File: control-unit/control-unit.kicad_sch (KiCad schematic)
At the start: 23 parts

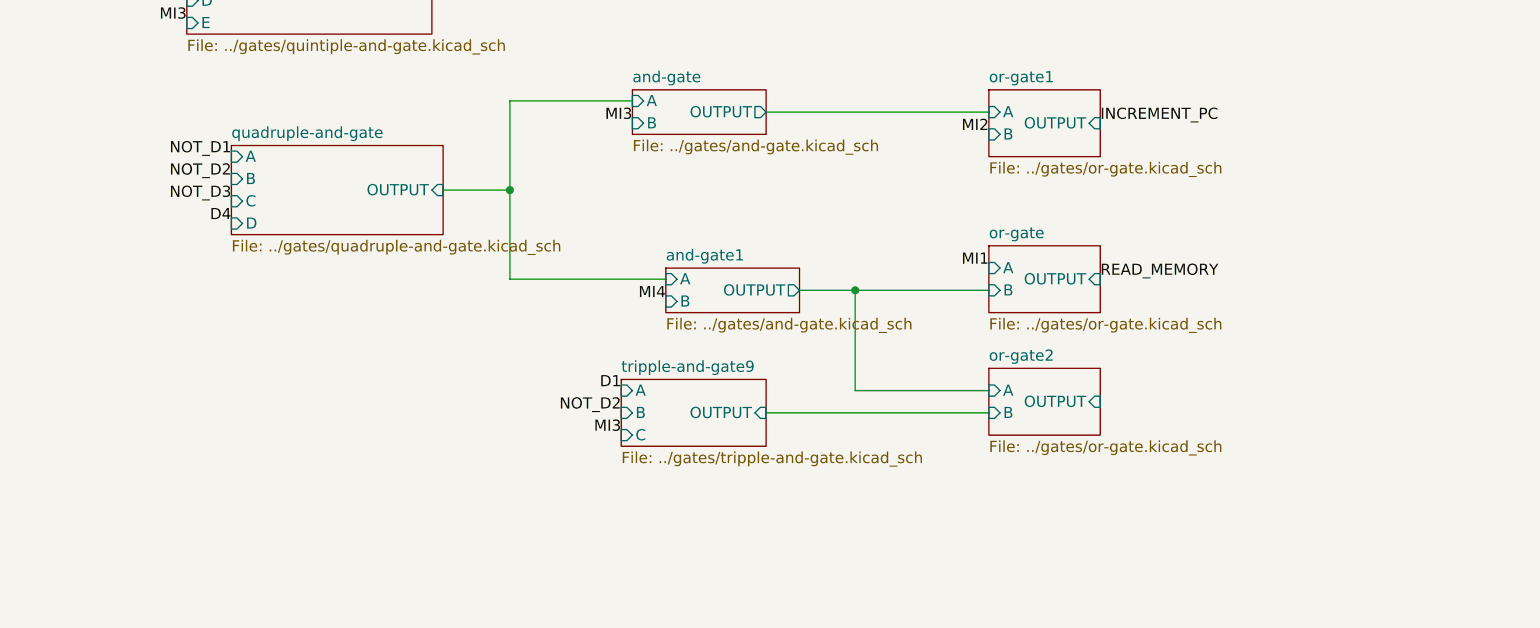
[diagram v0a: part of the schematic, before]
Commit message: Fix ADD command logic for control-unit
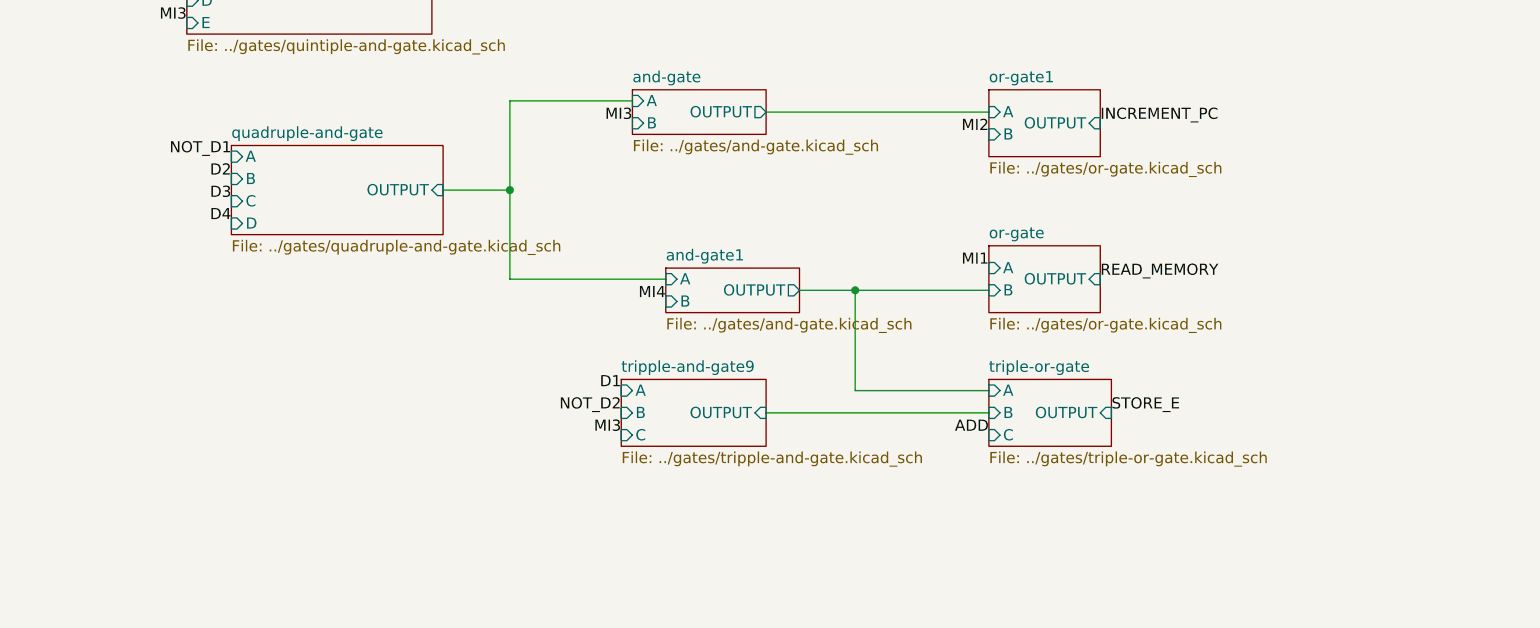
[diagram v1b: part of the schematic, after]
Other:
- removed sheet or-gate2
- added sheet triple-or-gate (../gates/triple-or-gate.kicad_sch)
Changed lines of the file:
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@@
 		)
 	)
+	(label "D2"
+		(at 135.89 114.3 180)
+		(fields_autoplaced yes)
+		(effects
+			(font
+				(size 1.27 1.27)
+			)
+			(justify right bottom)
+		)
+	)
 	(label "MI3"
 		(at 62.23 113.03 180)
@@
 		)
 	)
-	(label "NOT_D3"
-		(at 135.89 116.84 180)
-		(fields_autoplaced yes)
-		(effects
-			(font
-				(size 1.27 1.27)
-			)
-			(justify right bottom)
-		)
-	)
 	(label "MI4"
 		(at 121.92 30.48 0)
@@
 		)
 	)
+	(label "ADD"
+		(at 222.25 143.51 180)
+		(fields_autoplaced yes)
+		(effects
+			(font
+				(size 1.27 1.27)
+			)
+			(justify right bottom)
+		)
+	)
 	(label "STORE"
 		(at 257.81 60.96 180)
@@
 		)
 	)
-	(label "NOT_D2"
-		(at 135.89 114.3 180)
+	(label "STORE_E"
+		(at 236.22 140.97 0)
 		(fields_autoplaced yes)
 		(effects
@@
 				(size 1.27 1.27)
 			)
-			(justify right bottom)
+			(justify left bottom)
 		)
 	)
@@
 		)
 	)
+	(label "D3"
+		(at 135.89 116.84 180)
+		(fields_autoplaced yes)
+		(effects
+			(font
+				(size 1.27 1.27)
+			)
+			(justify right bottom)
+		)
+	)
 	(label "MI3"
 		(at 121.92 27.94 0)
@@
 	)
 	(sheet
-		(at 62.23 144.78)
-		(size 16.51 7.62)
+		(at 222.25 137.16)
+		(size 13.97 7.62)
 		(fields_autoplaced yes)
 		(stroke
@@
 			(color 0 0 0 0.0000)
 		)
-		(property "Sheetname" "tripple-and-gate4"
-			(at 62.23 144.0684 0)
+		(property "Sheetname" "triple-or-gate"
+			(at 222.25 136.4484 0)
 			(effects
 				(font
@@
 			)
 		)
-		(property "Sheetfile" "../gates/tripple-and-gate.kicad_sch"
-			(at 62.23 152.9846 0)
+		(property "Sheetfile" "../gates/triple-or-gate.kicad_sch"
+			(at 222.25 145.3646 0)
 			(effects
 				(font
@@
 			)
 		)
-		(pin "B" input
-			(at 62.23 148.59 180)
+		(pin "C" input
+			(at 222.25 143.51 180)
 			(effects
 				(font
@@
 			)
 		)
-		(pin "C" input
-			(at 62.23 151.13 180)
+		(pin "A" input
+			(at 222.25 138.43 180)
 			(effects
 				(font
@@
 		)
 		(pin "OUTPUT" input
-			(at 78.74 148.59 0)
+			(at 236.22 140.97 0)
 			(effects
 				(font
@@
 			)
 		)
-		(pin "A" input
-			(at 62.23 146.05 180)
+		(pin "B" input
+			(at 222.25 140.97 180)
 			(effects
 				(font
@@
 			(project "control-unit"
 				(path "/1cf3a7ee-ec47-45b6-b515-1840d726ab8f"
-					(page "7")
+					(page "36")
 				)
 			)
@@
 	)
 	(sheet
-		(at 222.25 135.89)
-		(size 12.7 7.62)
+		(at 62.23 144.78)
+		(size 16.51 7.62)
 		(fields_autoplaced yes)
 		(stroke
@@
 			(color 0 0 0 0.0000)
 		)
-		(property "Sheetname" "or-gate2"
-			(at 222.25 135.1784 0)
+		(property "Sheetname" "tripple-and-gate4"
+			(at 62.23 144.0684 0)
 			(effects
 				(font
@@
 			)
 		)
-		(property "Sheetfile" "../gates/or-gate.kicad_sch"
-			(at 222.25 144.0946 0)
+		(property "Sheetfile" "../gates/tripple-and-gate.kicad_sch"
+			(at 62.23 152.9846 0)
 			(effects
 				(font
@@
 			)
 		)
-		(pin "OUTPUT" input
-			(at 234.95 139.7 0)
+		(pin "B" input
+			(at 62.23 148.59 180)
 			(effects
 				(font
 					(size 1.27 1.27)
 				)
-				(justify right)
+				(justify left)
 			)
 		)
-		(pin "A" input
-			(at 222.25 138.43 180)
+		(pin "C" input
+			(at 62.23 151.13 180)
 			(effects
 				(font
@@
 			)
 		)
-		(pin "B" input
-			(at 222.25 140.97 180)
+		(pin "OUTPUT" input
+			(at 78.74 148.59 0)
+			(effects
+				(font
+					(size 1.27 1.27)
+				)
+				(justify right)
+			)
+		)
+		(pin "A" input
+			(at 62.23 146.05 180)
 			(effects
 				(font
@@
 			(project "control-unit"
 				(path "/1cf3a7ee-ec47-45b6-b515-1840d726ab8f"
-					(page "23")
+					(page "7")
 				)
 			)

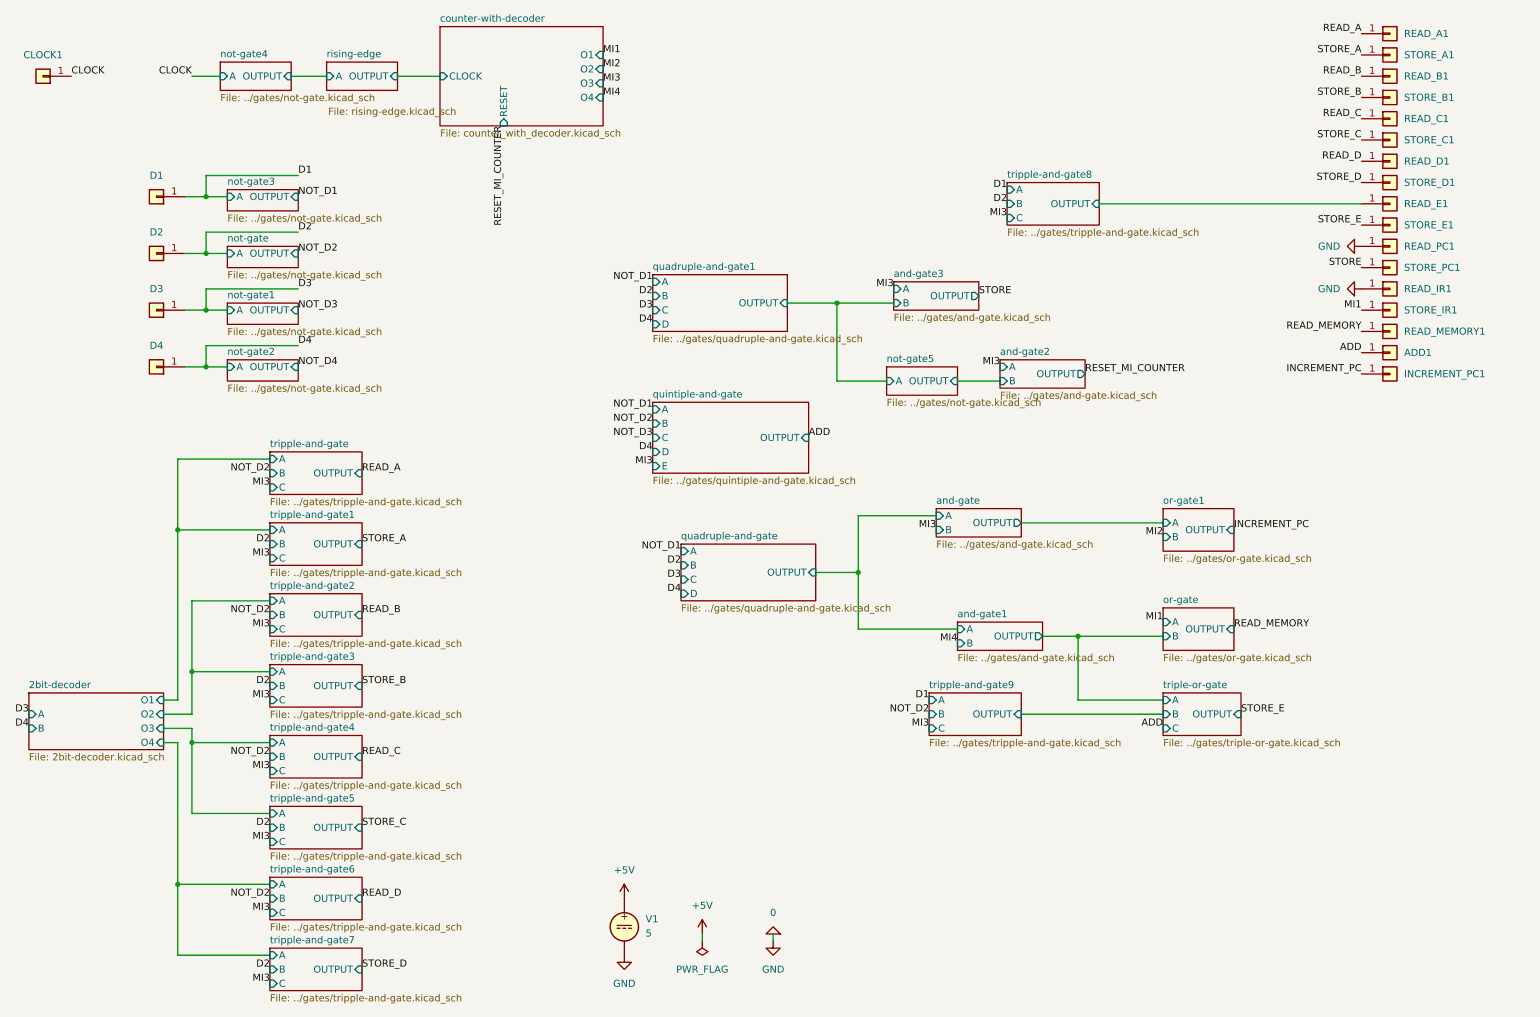
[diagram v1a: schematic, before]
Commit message: Implement logic for jump instruction
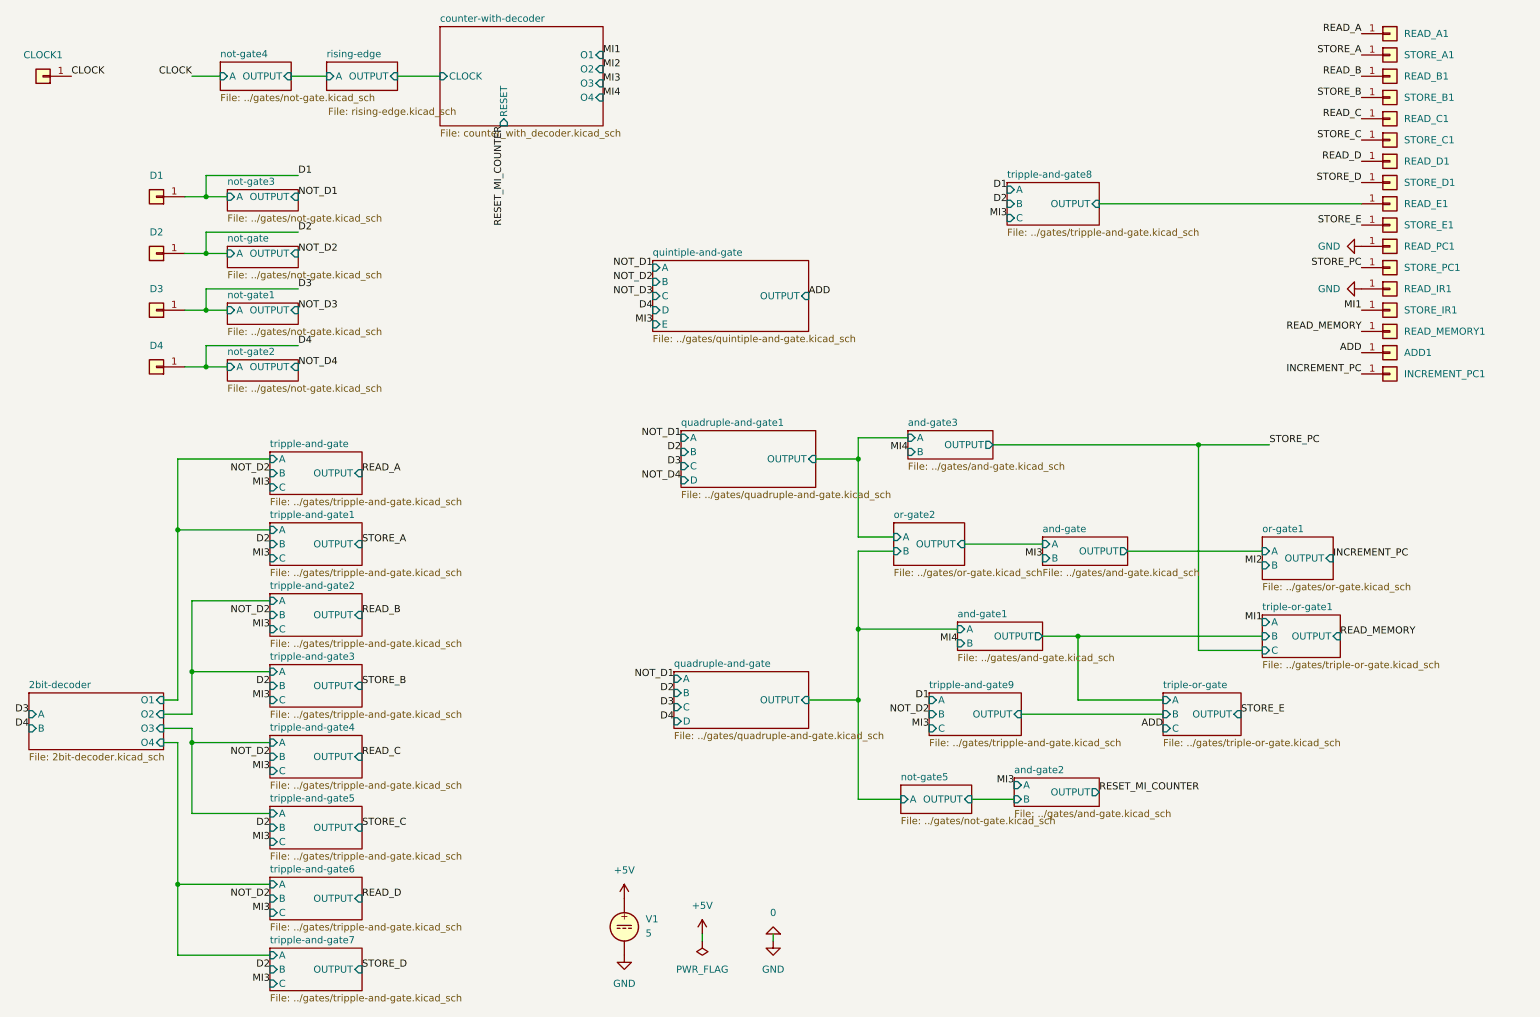
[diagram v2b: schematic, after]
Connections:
- net STORE renamed STORE_PC
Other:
- removed sheet or-gate
- added sheet or-gate2 (../gates/or-gate.kicad_sch)
- added sheet triple-or-gate1 (../gates/triple-or-gate.kicad_sch)
